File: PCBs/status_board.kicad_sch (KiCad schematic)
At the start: 19 parts, among them J1 Conn_01x03, J2 Conn_01x03, J3 Conn_01x02, J4 Conn_01x04, J5 Conn_01x04, J6 Conn_01x02, U1 XIAO-ESP32-S3-SMD

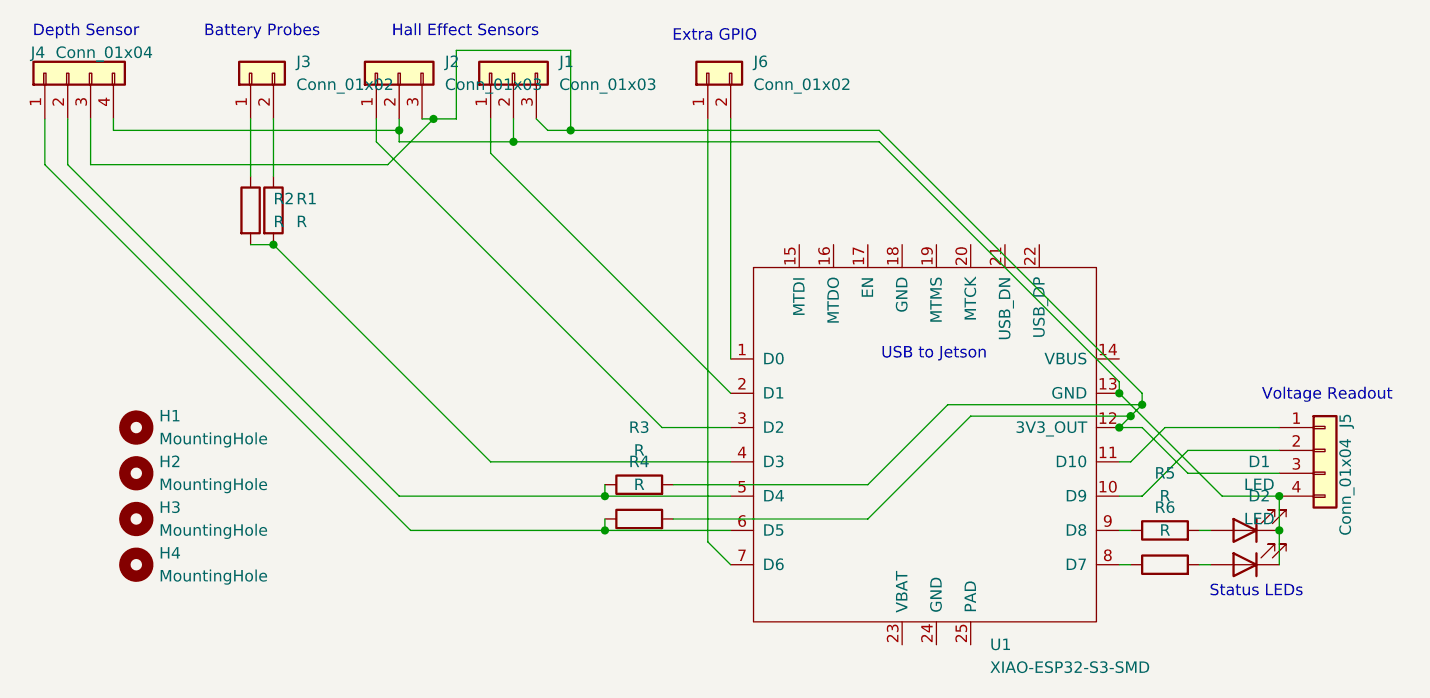
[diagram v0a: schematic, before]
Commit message: testing code + gnd to bat. (-) + gnd plane
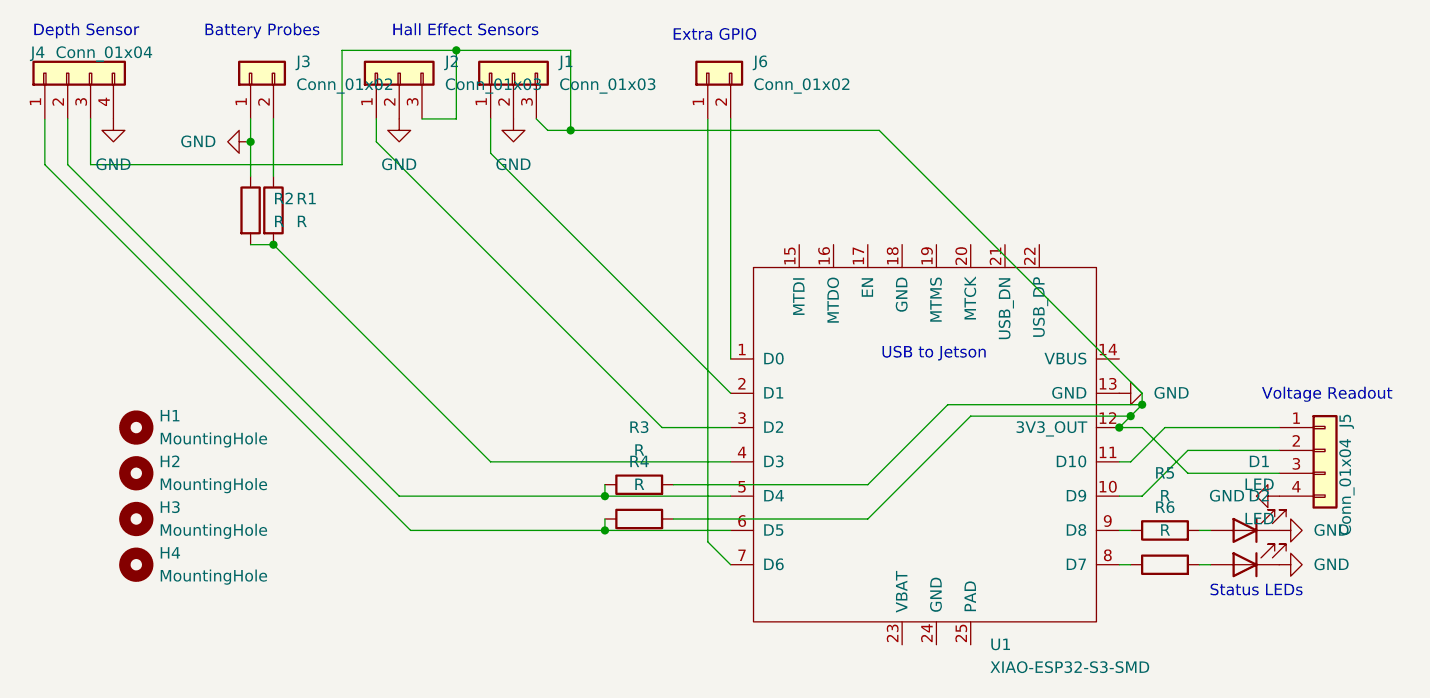
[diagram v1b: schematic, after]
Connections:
- net GND: now reaches J3.1 (Pin_1), R2.1
- net GND: now also D1.1 (K), D2.1 (K), J1.2 (Pin_2), J2.2 (Pin_2), J4.4 (Pin_4), J5.4 (Pin_4), U1.13 (GND)
